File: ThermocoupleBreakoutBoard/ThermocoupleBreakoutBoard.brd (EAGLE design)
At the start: 160 x 100 mm, 9 parts

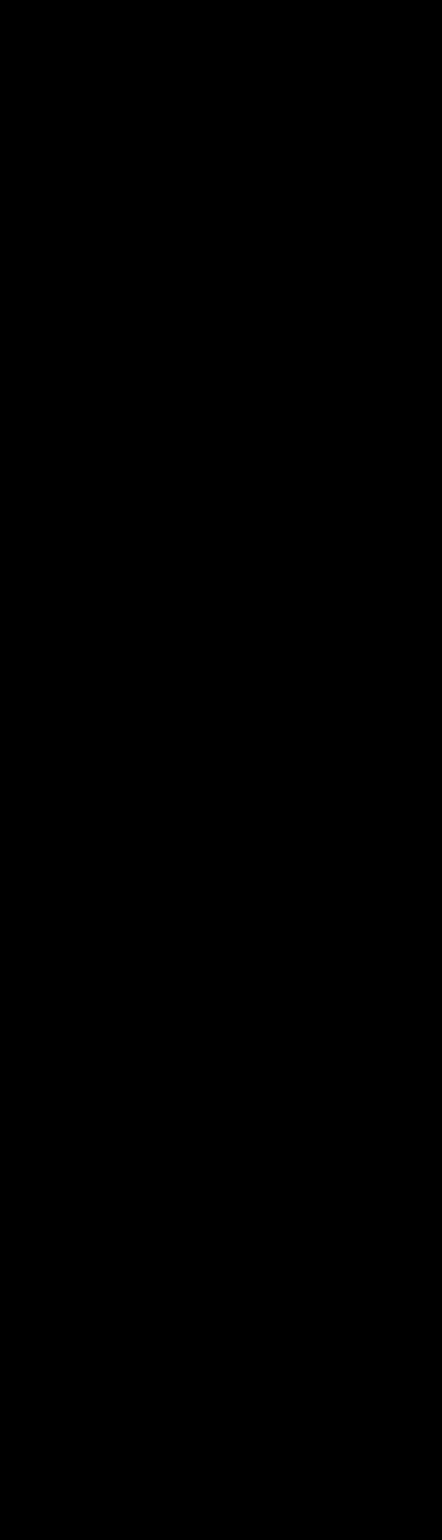
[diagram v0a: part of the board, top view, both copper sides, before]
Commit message: Duplicated 4-thermocouple input section
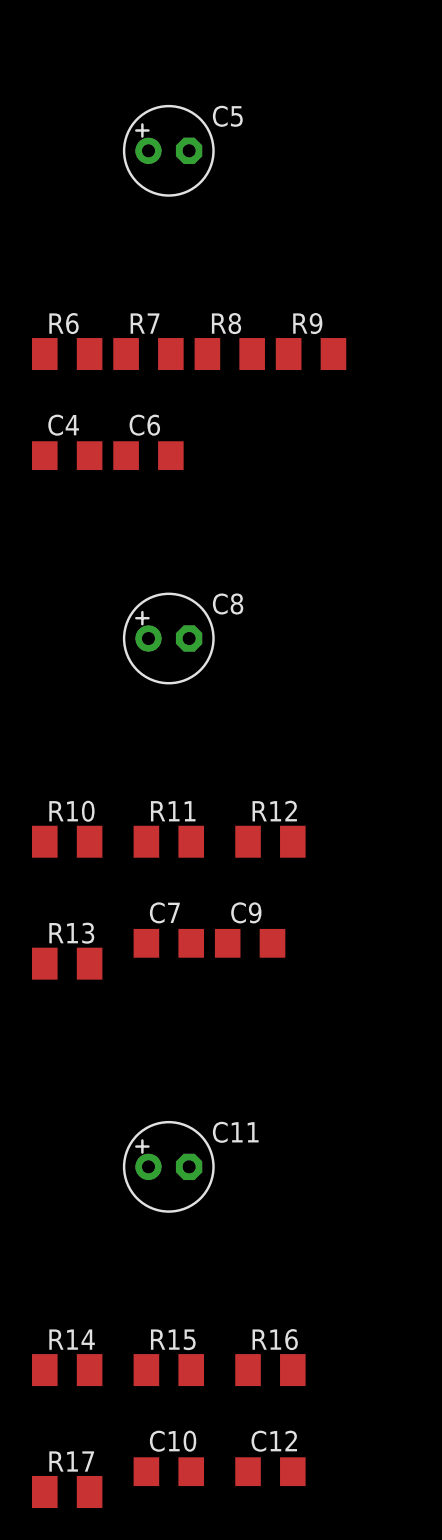
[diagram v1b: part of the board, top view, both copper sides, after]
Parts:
- added C10, C12, C4, C6, C7, C9: 104, rcl_vm:C1206
- added C11, C5, C8: 1uF, rcl_vm:E2,5-6
- added R10, R11, R14, R15, R6, R7: 1M, rcl_vm:M1206
- added R12, R13, R16, R17, R8, R9: 500, rcl_vm:M1206
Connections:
- net CH+ renamed 1-CH+
- net CH- renamed 1-CH-
- net TC+ renamed 1-TC+
- net TC- renamed 1-TC-
- removed net N$5: JP1.2, R1.2
- new net 2-CH+: C7.2, C8.+, R12.1
- new net 2-CH-: C8.-, C9.1, R13.1
- new net 2-TC+: R10.1, R12.2
- new net 2-TC-: R11.2, R13.2
- new net 3-CH+: C4.2, C5.+, R8.1
- new net 3-CH-: C5.-, C6.1, R9.1
- new net 3-TC+: R6.1, R8.2
- new net 3-TC-: R7.2, R9.2
- new net 4-CH+: C10.2, C11.+, R16.1
- new net 4-CH-: C11.-, C12.1, R17.1
- new net 4-TC+: R14.1, R16.2
- new net 4-TC-: R15.2, R17.2
- new net JP1-2: JP1.2, R1.2, R10.2, R14.2, R6.2
- net AGND: now also C10.1, C12.2, C4.1, C6.2, C7.1, C9.2, R11.1, R15.1, R7.1
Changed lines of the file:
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@@
 <element name="R4" library="rcl_vm" package="M1206" value="500" x="-25.4" y="17.78"/>
 <element name="R5" library="rcl_vm" package="M1206" value="10K" x="-15.24" y="24.13"/>
+<element name="C4" library="rcl_vm" package="C1206" value="104" x="-34.29" y="-31.75"/>
+<element name="R6" library="rcl_vm" package="M1206" value="1M" x="-34.29" y="-25.4"/>
+<element name="R7" library="rcl_vm" package="M1206" value="1M" x="-29.21" y="-25.4"/>
+<element name="R8" library="rcl_vm" package="M1206" value="500" x="-24.13" y="-25.4"/>
+<element name="R9" library="rcl_vm" package="M1206" value="500" x="-19.05" y="-25.4"/>
+<element name="C5" library="rcl_vm" package="E2,5-6" value="1uF" x="-27.94" y="-12.7"/>
+<element name="C6" library="rcl_vm" package="C1206" value="104" x="-29.21" y="-31.75"/>
+<element name="C7" library="rcl_vm" package="C1206" value="104" x="-27.94" y="-62.23"/>
+<element name="R10" library="rcl_vm" package="M1206" value="1M" x="-34.29" y="-55.88"/>
+<element name="R11" library="rcl_vm" package="M1206" value="1M" x="-27.94" y="-55.88"/>
+<element name="R12" library="rcl_vm" package="M1206" value="500" x="-21.59" y="-55.88"/>
+<element name="R13" library="rcl_vm" package="M1206" value="500" x="-34.29" y="-63.5"/>
+<element name="C8" library="rcl_vm" package="E2,5-6" value="1uF" x="-27.94" y="-43.18"/>
+<element name="C9" library="rcl_vm" package="C1206" value="104" x="-22.86" y="-62.23"/>
+<element name="C10" library="rcl_vm" package="C1206" value="104" x="-27.94" y="-95.25"/>
+<element name="R14" library="rcl_vm" package="M1206" value="1M" x="-34.29" y="-88.9"/>
+<element name="R15" library="rcl_vm" package="M1206" value="1M" x="-27.94" y="-88.9"/>
+<element name="R16" library="rcl_vm" package="M1206" value="500" x="-21.59" y="-88.9"/>
+<element name="R17" library="rcl_vm" package="M1206" value="500" x="-34.29" y="-96.52"/>
+<element name="C11" library="rcl_vm" package="E2,5-6" value="1uF" x="-27.94" y="-76.2"/>
+<element name="C12" library="rcl_vm" package="C1206" value="104" x="-21.59" y="-95.25"/>
 </elements>
 <signals>
-<signal name="TC+">
-<contactref element="R1" pad="1"/>
-<contactref element="R3" pad="2"/>
-<wire x1="-18.92" y1="17.78" x2="-26.8" y2="11.43" width="0" layer="19" extent="1-1"/>
+<signal name="4-TC+">
+<contactref element="R14" pad="1"/>
+<contactref element="R16" pad="2"/>
+<wire x1="-20.19" y1="-88.9" x2="-35.69" y2="-88.9" width="0" layer="19" extent="1-1"/>
 </signal>
-<signal name="TC-">
-<contactref element="R2" pad="2"/>
-<contactref element="R4" pad="2"/>
-<wire x1="-24" y1="17.78" x2="-13.84" y2="17.78" width="0" layer="19" extent="1-1"/>
+<signal name="4-TC-">
+<contactref element="R15" pad="2"/>
+<contactref element="R17" pad="2"/>
+<wire x1="-26.54" y1="-88.9" x2="-32.89" y2="-96.52" width="0" layer="19" extent="1-1"/>
 </signal>
-<signal name="CH-">
-<contactref element="R4" pad="1"/>
-<contactref element="C2" pad="-"/>
-<contactref element="C3" pad="1"/>
-<wire x1="-21.72" y1="11.43" x2="-26.67" y2="3.81" width="0" layer="19" extent="1-1"/>
-<wire x1="-26.8" y1="17.78" x2="-21.72" y2="11.43" width="0" layer="19" extent="1-1"/>
+<signal name="4-CH-">
+<contactref element="R17" pad="1"/>
+<contactref element="C11" pad="-"/>
+<contactref element="C12" pad="1"/>
+<wire x1="-22.99" y1="-95.25" x2="-35.69" y2="-96.52" width="0" layer="19" extent="1-1"/>
+<wire x1="-26.67" y1="-76.2" x2="-22.99" y2="-95.25" width="0" layer="19" extent="1-1"/>
 </signal>
-<signal name="CH+">
-<contactref element="R3" pad="1"/>
-<contactref element="C2" pad="+"/>
-<contactref element="C1" pad="2"/>
-<wire x1="-21.72" y1="17.78" x2="-29.21" y2="3.81" width="0" layer="19" extent="1-1"/>
-<wire x1="-13.84" y1="11.43" x2="-21.72" y2="17.78" width="0" layer="19" extent="1-1"/>
-</signal>
-<signal name="N$5">
-<contactref element="R1" pad="2"/>
-<contactref element="JP1" pad="2"/>
-<wire x1="-24" y1="11.43" x2="-17.78" y2="3.81" width="0" layer="19" extent="1-1"/>
+<signal name="4-CH+">
+<contactref element="R16" pad="1"/>
+<contactref element="C11" pad="+"/>
+<contactref element="C10" pad="2"/>
+<wire x1="-22.99" y1="-88.9" x2="-26.54" y2="-95.25" width="0" layer="19" extent="1-1"/>
+<wire x1="-29.21" y1="-76.2" x2="-22.99" y2="-88.9" width="0" layer="19" extent="1-1"/>
 </signal>
 <signal name="+3V3">
@@
 <contactref element="C3" pad="2"/>
 <contactref element="R2" pad="1"/>
-<wire x1="-16.64" y1="17.78" x2="-13.84" y2="24.13" width="0" layer="19" extent="1-1"/>
-<wire x1="-16.64" y1="11.43" x2="-16.64" y2="17.78" width="0" layer="19" extent="1-1"/>
-<wire x1="-18.92" y1="11.43" x2="-16.64" y2="11.43" width="0" layer="19" extent="1-1"/>
+<contactref element="C4" pad="1"/>
+<contactref element="C6" pad="2"/>
+<contactref element="R7" pad="1"/>
+<contactref element="C7" pad="1"/>
+<contactref element="C9" pad="2"/>
+<contactref element="R11" pad="1"/>
+<contactref element="C10" pad="1"/>
+<contactref element="C12" pad="2"/>
+<contactref element="R15" pad="1"/>
+<wire x1="-29.34" y1="-88.9" x2="-29.34" y2="-95.25" width="0" layer="19" extent="1-1"/>
+<wire x1="-20.19" y1="-95.25" x2="-29.34" y2="-95.25" width="0" layer="19" extent="1-1"/>
+<wire x1="-29.34" y1="-62.23" x2="-29.34" y2="-88.9" width="0" layer="19" extent="1-1"/>
+<wire x1="-29.34" y1="-55.88" x2="-29.34" y2="-62.23" width="0" layer="19" extent="1-1"/>
+<wire x1="-21.46" y1="-62.23" x2="-29.34" y2="-62.23" width="0" layer="19" extent="1-1"/>
+<wire x1="-27.81" y1="-31.75" x2="-29.34" y2="-55.88" width="0" layer="19" extent="1-1"/>
+<wire x1="-30.61" y1="-25.4" x2="-27.81" y2="-31.75" width="0" layer="19" extent="1-1"/>
+<wire x1="-35.69" y1="-31.75" x2="-27.81" y2="-31.75" width="0" layer="19" extent="1-1"/>
+<wire x1="-18.92" y1="11.43" x2="-30.61" y2="-25.4" width="0" layer="19" extent="1-1"/>
+<wire x1="-16.64" y1="11.43" x2="-18.92" y2="11.43" width="0" layer="19" extent="1-1"/>
+<wire x1="-16.64" y1="17.78" x2="-16.64" y2="11.43" width="0" layer="19" extent="1-1"/>
+<wire x1="-13.84" y1="24.13" x2="-16.64" y2="17.78" width="0" layer="19" extent="1-1"/>
+</signal>
+<signal name="JP1-2">
+<contactref element="R1" pad="2"/>
+<contactref element="JP1" pad="2"/>
+<contactref element="R6" pad="2"/>
+<contactref element="R10" pad="2"/>
+<contactref element="R14" pad="2"/>
+<wire x1="-32.89" y1="-55.88" x2="-32.89" y2="-88.9" width="0" layer="19" extent="1-1"/>
+<wire x1="-32.89" y1="-25.4" x2="-32.89" y2="-55.88" width="0" layer="19" extent="1-1"/>
+<wire x1="-17.78" y1="3.81" x2="-32.89" y2="-25.4" width="0" layer="19" extent="1-1"/>
+<wire x1="-24" y1="11.43" x2="-17.78" y2="3.81" width="0" layer="19" extent="1-1"/>
+</signal>
+<signal name="1-TC+">
+<contactref element="R1" pad="1"/>
+<contactref element="R3" pad="2"/>
+<wire x1="-18.92" y1="17.78" x2="-26.8" y2="11.43" width="0" layer="19" extent="1-1"/>
+</signal>
+<signal name="1-TC-">
+<contactref element="R2" pad="2"/>
+<contactref element="R4" pad="2"/>
+<wire x1="-24" y1="17.78" x2="-13.84" y2="17.78" width="0" layer="19" extent="1-1"/>
+</signal>
+<signal name="2-TC+">
+<contactref element="R10" pad="1"/>
+<contactref element="R12" pad="2"/>
+<wire x1="-20.19" y1="-55.88" x2="-35.69" y2="-55.88" width="0" layer="19" extent="1-1"/>
+</signal>
+<signal name="2-TC-">
+<contactref element="R11" pad="2"/>
+<contactref element="R13" pad="2"/>
+<wire x1="-26.54" y1="-55.88" x2="-32.89" y2="-63.5" width="0" layer="19" extent="1-1"/>
+</signal>
+<signal name="3-TC+">
+<contactref element="R6" pad="1"/>
+<contactref element="R8" pad="2"/>
+<wire x1="-22.73" y1="-25.4" x2="-35.69" y2="-25.4" width="0" layer="19" extent="1-1"/>
+</signal>
+<signal name="3-TC-">
+<contactref element="R7" pad="2"/>
+<contactref element="R9" pad="2"/>
+<wire x1="-17.65" y1="-25.4" x2="-27.81" y2="-25.4" width="0" layer="19" extent="1-1"/>
+</signal>
+<signal name="1-CH+">
+<contactref element="R3" pad="1"/>
+<contactref element="C2" pad="+"/>
+<contactref element="C1" pad="2"/>
+<wire x1="-21.72" y1="17.78" x2="-29.21" y2="3.81" width="0" layer="19" extent="1-1"/>
+<wire x1="-13.84" y1="11.43" x2="-21.72" y2="17.78" width="0" layer="19" extent="1-1"/>
+</signal>
+<signal name="1-CH-">
+<contactref element="R4" pad="1"/>
+<contactref element="C2" pad="-"/>
+<contactref element="C3" pad="1"/>
+<wire x1="-21.72" y1="11.43" x2="-26.67" y2="3.81" width="0" layer="19" extent="1-1"/>
+<wire x1="-26.8" y1="17.78" x2="-21.72" y2="11.43" width="0" layer="19" extent="1-1"/>
+</signal>
+<signal name="2-CH+">
+<contactref element="R12" pad="1"/>
+<contactref element="C8" pad="+"/>
+<contactref element="C7" pad="2"/>
+<wire x1="-22.99" y1="-55.88" x2="-26.54" y2="-62.23" width="0" layer="19" extent="1-1"/>
+<wire x1="-29.21" y1="-43.18" x2="-22.99" y2="-55.88" width="0" layer="19" extent="1-1"/>
+</signal>
+<signal name="2-CH-">
+<contactref element="R13" pad="1"/>
+<contactref element="C8" pad="-"/>
+<contactref element="C9" pad="1"/>
+<wire x1="-24.26" y1="-62.23" x2="-35.69" y2="-63.5" width="0" layer="19" extent="1-1"/>
+<wire x1="-26.67" y1="-43.18" x2="-24.26" y2="-62.23" width="0" layer="19" extent="1-1"/>
+</signal>
+<signal name="3-CH+">
+<contactref element="R8" pad="1"/>
+<contactref element="C5" pad="+"/>
+<contactref element="C4" pad="2"/>
+<wire x1="-25.53" y1="-25.4" x2="-32.89" y2="-31.75" width="0" layer="19" extent="1-1"/>
+<wire x1="-29.21" y1="-12.7" x2="-25.53" y2="-25.4" width="0" layer="19" extent="1-1"/>
+</signal>
+<signal name="3-CH-">
+<contactref element="R9" pad="1"/>
+<contactref element="C5" pad="-"/>
+<contactref element="C6" pad="1"/>
+<wire x1="-20.45" y1="-25.4" x2="-30.61" y2="-31.75" width="0" layer="19" extent="1-1"/>
+<wire x1="-26.67" y1="-12.7" x2="-20.45" y2="-25.4" width="0" layer="19" extent="1-1"/>
 </signal>
 </signals>

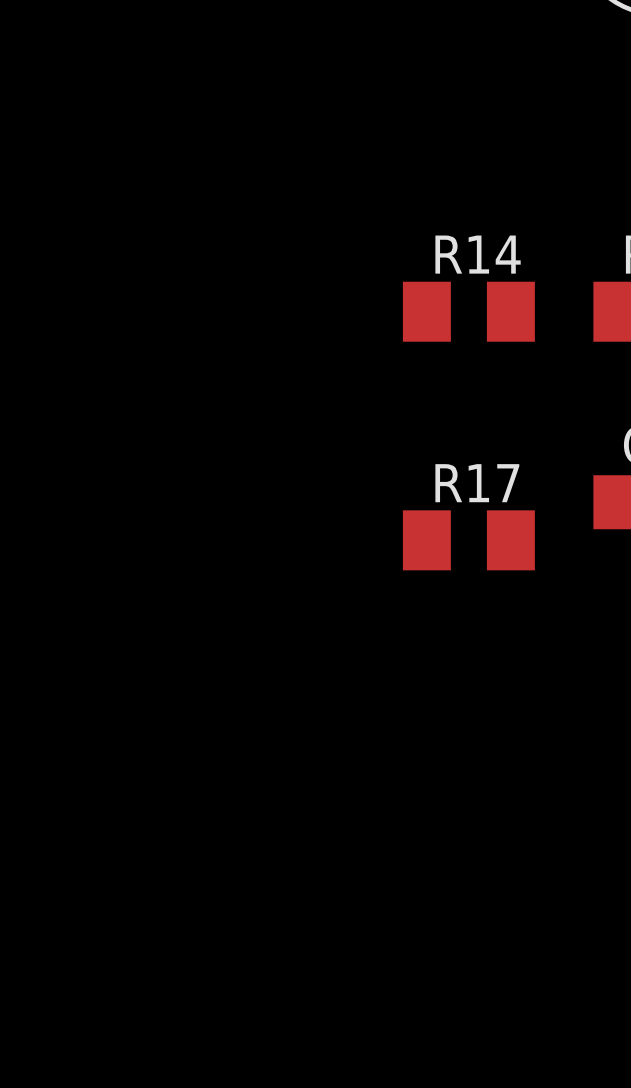
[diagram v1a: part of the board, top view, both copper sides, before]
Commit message: Added MCP3424 Device and made routing
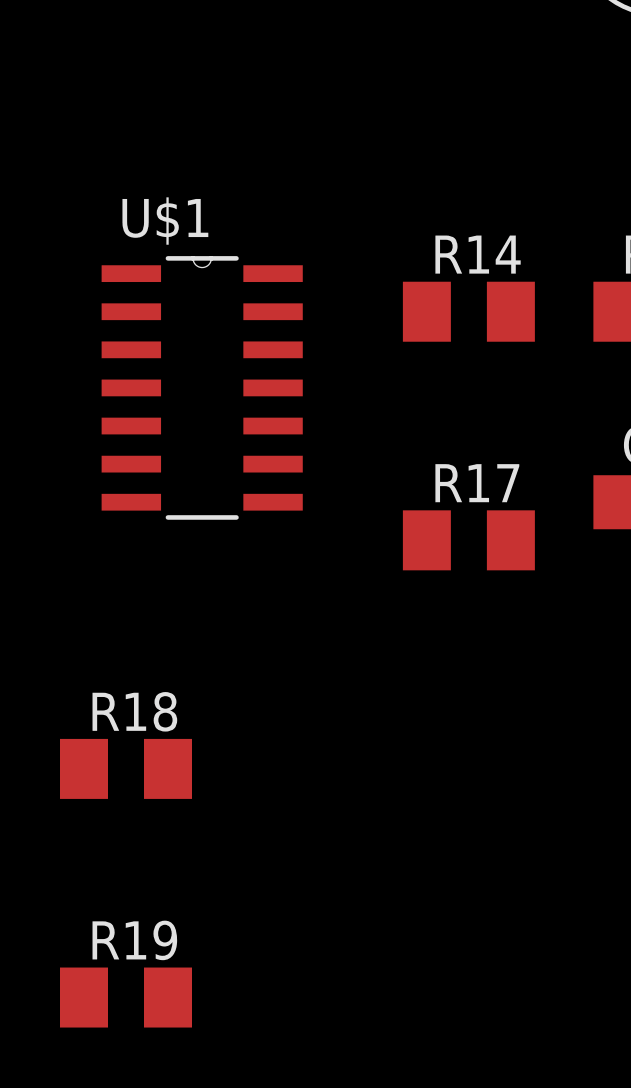
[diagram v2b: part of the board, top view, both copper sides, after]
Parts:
- added R18, R19: 500, rcl_vm:M1206
- added U$1: MCP3424-E/SL, i2c_devices:SOIC127P600X175-14N
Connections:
- new net N$1: R18.2, U$1.8
- new net N$2: R19.2, U$1.7
- net 1-CH+: now also U$1.1
- net 1-CH-: now also U$1.2
- net 2-CH+: now also U$1.3
- net 2-CH-: now also U$1.4
- net 3-CH+: now also U$1.11
- net 3-CH-: now also U$1.12
- net 4-CH+: now also U$1.13
- net 4-CH-: now also U$1.14
- net GND: now also U$1.5
- net JP1-2: now also R18.1, R19.1, U$1.6
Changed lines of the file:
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@@
 <element name="C11" library="rcl_vm" package="E2,5-6" value="1uF" x="-27.94" y="-76.2"/>
 <element name="C12" library="rcl_vm" package="C1206" value="104" x="-21.59" y="-95.25"/>
+<element name="U$1" library="i2c_devices" package="SOIC127P600X175-14N" value="MCP3424-E/SL" x="-43.18" y="-91.44">
+<attribute name="SUPPLIER" value="Microchip" x="-43.18" y="-91.44" size="1.778" layer="27" display="off"/>
+<attribute name="OC_FARNELL" value="1630424" x="-43.18" y="-91.44" size="1.778" layer="27" display="off"/>
+<attribute name="MPN" value="MCP3424-E/SL" x="-43.18" y="-91.44" size="1.778" layer="27" display="off"/>
+<attribute name="PACKAGE" value="SOIC-14" x="-43.18" y="-91.44" size="1.778" layer="27" display="off"/>
+<attribute name="OC_NEWARK" value="54M4871" x="-43.18" y="-91.44" size="1.778" layer="27" display="off"/>
+</element>
+<element name="R18" library="rcl_vm" package="M1206" value="500" x="-45.72" y="-104.14"/>
+<element name="R19" library="rcl_vm" package="M1206" value="500" x="-45.72" y="-111.76"/>
 </elements>
 <signals>
@@
 <contactref element="C11" pad="-"/>
 <contactref element="C12" pad="1"/>
+<contactref element="U$1" pad="14"/>
+<wire x1="-40.8178" y1="-87.63" x2="-35.69" y2="-96.52" width="0" layer="19" extent="1-1"/>
 <wire x1="-22.99" y1="-95.25" x2="-35.69" y2="-96.52" width="0" layer="19" extent="1-1"/>
-<wire x1="-26.67" y1="-76.2" x2="-22.99" y2="-95.25" width="0" layer="19" extent="1-1"/>
+<wire x1="-26.67" y1="-76.2" x2="-40.8178" y2="-87.63" width="0" layer="19" extent="1-1"/>
 </signal>
 <signal name="4-CH+">
@@
 <contactref element="C11" pad="+"/>
 <contactref element="C10" pad="2"/>
+<contactref element="U$1" pad="13"/>
+<wire x1="-26.54" y1="-95.25" x2="-40.8178" y2="-88.9" width="0" layer="19" extent="1-1"/>
 <wire x1="-22.99" y1="-88.9" x2="-26.54" y2="-95.25" width="0" layer="19" extent="1-1"/>
 <wire x1="-29.21" y1="-76.2" x2="-22.99" y2="-88.9" width="0" layer="19" extent="1-1"/>
@@
 <signal name="GND">
 <contactref element="R5" pad="1"/>
+<contactref element="U$1" pad="5"/>
+<wire x1="-16.64" y1="24.13" x2="-45.5422" y2="-92.71" width="0" layer="19" extent="1-1"/>
 </signal>
 <signal name="AGND">
@@
 <contactref element="R10" pad="2"/>
 <contactref element="R14" pad="2"/>
+<contactref element="U$1" pad="6"/>
+<contactref element="R18" pad="1"/>
+<contactref element="R19" pad="1"/>
+<wire x1="-47.12" y1="-104.14" x2="-47.12" y2="-111.76" width="0" layer="19" extent="1-1"/>
+<wire x1="-45.5422" y1="-93.98" x2="-47.12" y2="-104.14" width="0" layer="19" extent="1-1"/>
+<wire x1="-32.89" y1="-88.9" x2="-45.5422" y2="-93.98" width="0" layer="19" extent="1-1"/>
 <wire x1="-32.89" y1="-55.88" x2="-32.89" y2="-88.9" width="0" layer="19" extent="1-1"/>
 <wire x1="-32.89" y1="-25.4" x2="-32.89" y2="-55.88" width="0" layer="19" extent="1-1"/>
@@
 <contactref element="C2" pad="+"/>
 <contactref element="C1" pad="2"/>
+<contactref element="U$1" pad="1"/>
+<wire x1="-29.21" y1="3.81" x2="-45.5422" y2="-87.63" width="0" layer="19" extent="1-1"/>
 <wire x1="-21.72" y1="17.78" x2="-29.21" y2="3.81" width="0" layer="19" extent="1-1"/>
 <wire x1="-13.84" y1="11.43" x2="-21.72" y2="17.78" width="0" layer="19" extent="1-1"/>
@@
 <contactref element="C2" pad="-"/>
 <contactref element="C3" pad="1"/>
+<contactref element="U$1" pad="2"/>
+<wire x1="-26.67" y1="3.81" x2="-45.5422" y2="-88.9" width="0" layer="19" extent="1-1"/>
 <wire x1="-21.72" y1="11.43" x2="-26.67" y2="3.81" width="0" layer="19" extent="1-1"/>
 <wire x1="-26.8" y1="17.78" x2="-21.72" y2="11.43" width="0" layer="19" extent="1-1"/>
@@
 <contactref element="C8" pad="+"/>
 <contactref element="C7" pad="2"/>
+<contactref element="U$1" pad="3"/>
+<wire x1="-26.54" y1="-62.23" x2="-45.5422" y2="-90.17" width="0" layer="19" extent="1-1"/>
 <wire x1="-22.99" y1="-55.88" x2="-26.54" y2="-62.23" width="0" layer="19" extent="1-1"/>
 <wire x1="-29.21" y1="-43.18" x2="-22.99" y2="-55.88" width="0" layer="19" extent="1-1"/>
@@
 <contactref element="C8" pad="-"/>
 <contactref element="C9" pad="1"/>
+<contactref element="U$1" pad="4"/>
+<wire x1="-35.69" y1="-63.5" x2="-45.5422" y2="-91.44" width="0" layer="19" extent="1-1"/>
 <wire x1="-24.26" y1="-62.23" x2="-35.69" y2="-63.5" width="0" layer="19" extent="1-1"/>
 <wire x1="-26.67" y1="-43.18" x2="-24.26" y2="-62.23" width="0" layer="19" extent="1-1"/>
@@
 <contactref element="C5" pad="+"/>
 <contactref element="C4" pad="2"/>
+<contactref element="U$1" pad="11"/>
+<wire x1="-32.89" y1="-31.75" x2="-40.8178" y2="-91.44" width="0" layer="19" extent="1-1"/>
 <wire x1="-25.53" y1="-25.4" x2="-32.89" y2="-31.75" width="0" layer="19" extent="1-1"/>
 <wire x1="-29.21" y1="-12.7" x2="-25.53" y2="-25.4" width="0" layer="19" extent="1-1"/>
@@
 <contactref element="C5" pad="-"/>
 <contactref element="C6" pad="1"/>
+<contactref element="U$1" pad="12"/>
+<wire x1="-30.61" y1="-31.75" x2="-40.8178" y2="-90.17" width="0" layer="19" extent="1-1"/>
 <wire x1="-20.45" y1="-25.4" x2="-30.61" y2="-31.75" width="0" layer="19" extent="1-1"/>
 <wire x1="-26.67" y1="-12.7" x2="-20.45" y2="-25.4" width="0" layer="19" extent="1-1"/>
 </signal>
+<signal name="N$1">
+<contactref element="U$1" pad="8"/>
+<contactref element="R18" pad="2"/>
+<wire x1="-40.8178" y1="-95.25" x2="-44.32" y2="-104.14" width="0" layer="19" extent="1-1"/>
+</signal>
+<signal name="N$2">
+<contactref element="U$1" pad="7"/>
+<contactref element="R19" pad="2"/>
+<wire x1="-45.5422" y1="-95.25" x2="-44.32" y2="-111.76" width="0" layer="19" extent="1-1"/>
+</signal>
 </signals>
